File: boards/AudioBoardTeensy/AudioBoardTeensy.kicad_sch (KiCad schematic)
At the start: 7 parts, among them J1 AudioJack2_Ground, U1 Teensy4.0

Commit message: Schematic draft
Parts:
- added H1, H2, H3, H4: MountingHole_Pad, symbol Mechanical:MountingHole_Pad
- added J2, J3, J4: Conn_01x20_Pin, Connector_PinHeader_2.54mm:PinHeader_1x20_P2.54mm_Vertical, symbol Connector:Conn_01x20_Pin
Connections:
- net +3V3: now also J2.2 (Pin_2), J3.1 (Pin_1), J3.10 (Pin_10), J3.11 (Pin_11), J3.12 (Pin_12), J3.13 (Pin_13), J3.14 (Pin_14), J3.15 (Pin_15), J3.16 (Pin_16), J3.17 (Pin_17), J3.18 (Pin_18), J3.19 (Pin_19), J3.2 (Pin_2), J3.20 (Pin_20), J3.3 (Pin_3), J3.4 (Pin_4), J3.5 (Pin_5), J3.6 (Pin_6), J3.7 (Pin_7), J3.8 (Pin_8), J3.9 (Pin_9)
- net GND: now also J2.1 (Pin_1), J2.20 (Pin_20)
- net MOSI: now reaches U1.13 (11_MOSI_CTX1)
- net MOSI: now also J2.8 (Pin_8)
- net MISO: now reaches U1.14 (12_MISO_MQSL)
- net MISO: now also J2.4 (Pin_4)
- net CS: now reaches U1.2 (0_RX1_CRX2_CS1)
- net CS: now also J2.15 (Pin_15)
- net SCK: now reaches U1.20 (13_SCK_CRX1_LED)
- net SCK: now also J2.7 (Pin_7)
- net RST: now reaches U1.3 (1_TX1_CTX2_MISO1)
- net RST: now also J2.16 (Pin_16)
- new net LED1: J4.1 (Pin_1)
- new net LED10: J4.10 (Pin_10)
- new net LED11: J4.11 (Pin_11)
- new net LED12: J4.12 (Pin_12)
- new net LED13: J4.13 (Pin_13)
- new net LED14: J4.14 (Pin_14)
- new net LED15: J4.15 (Pin_15)
- new net LED16: J4.16 (Pin_16)
- new net LED17: J4.17 (Pin_17)
- new net LED18: J4.18 (Pin_18)
- new net LED19: J4.19 (Pin_19)
- new net LED2: J4.2 (Pin_2)
- new net LED20: J4.20 (Pin_20)
- new net LED3: J4.3 (Pin_3)
- new net LED4: J4.4 (Pin_4)
- new net LED5: J4.5 (Pin_5)
- new net LED6: J4.6 (Pin_6)
- new net LED7: J4.7 (Pin_7)
- new net LED8: J4.8 (Pin_8)
- new net LED9: J4.9 (Pin_9)
- no-connect marks 1 -> 17
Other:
- note added: "LEFT"
- note added: "MOUNT HOLES"
- note added: "RIGHT"
- moved on the sheet: U1

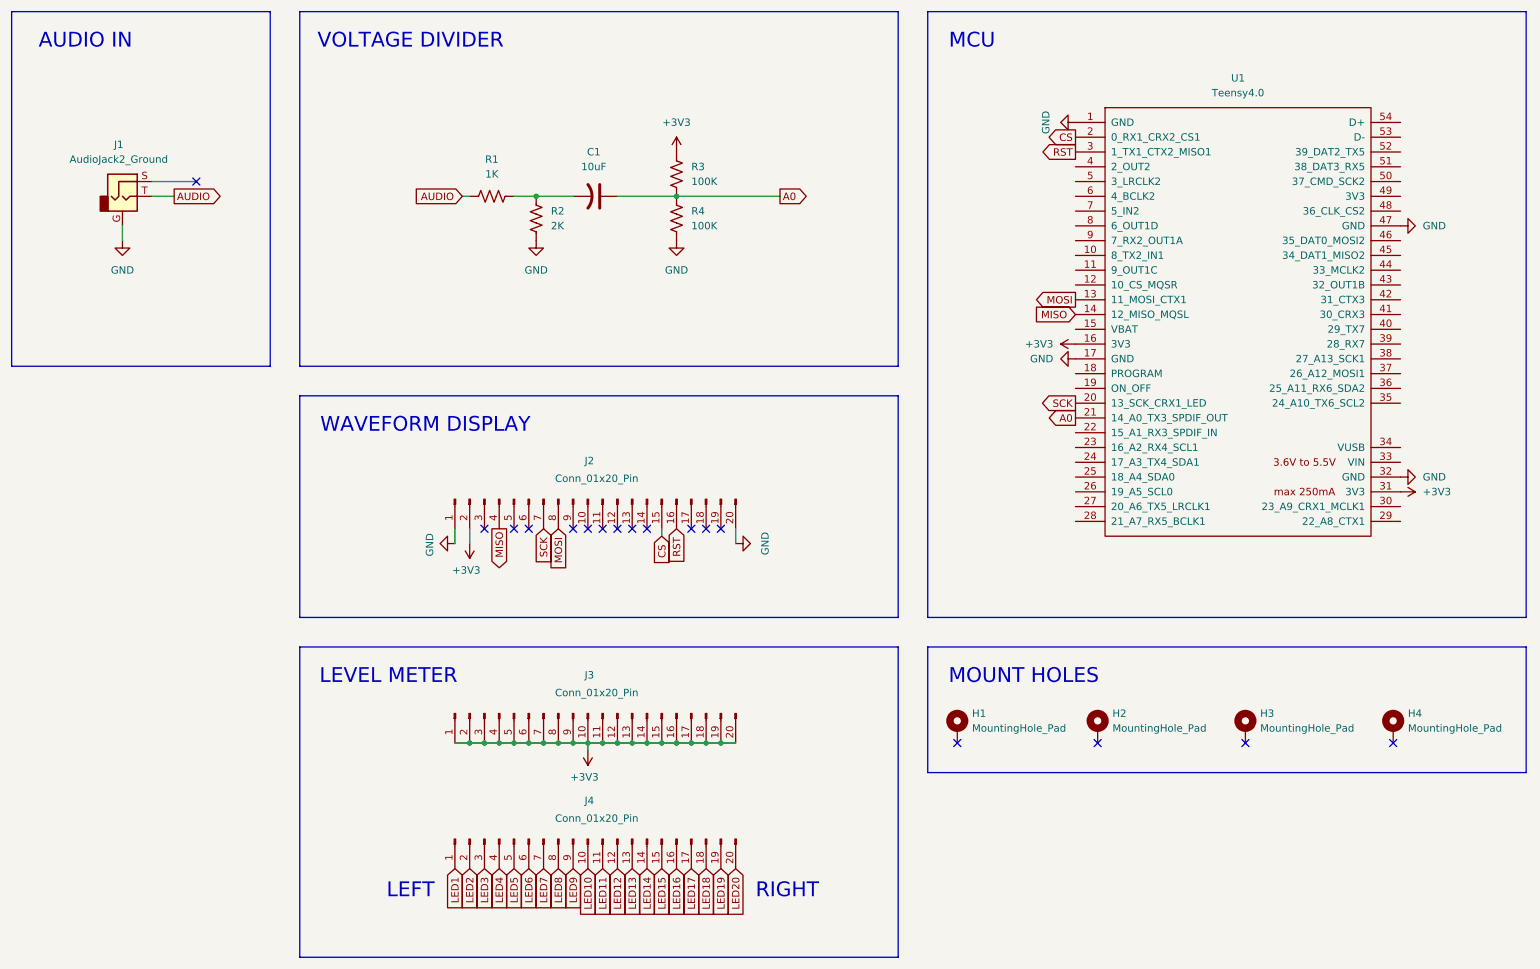
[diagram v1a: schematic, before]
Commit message: Develop audio board readme
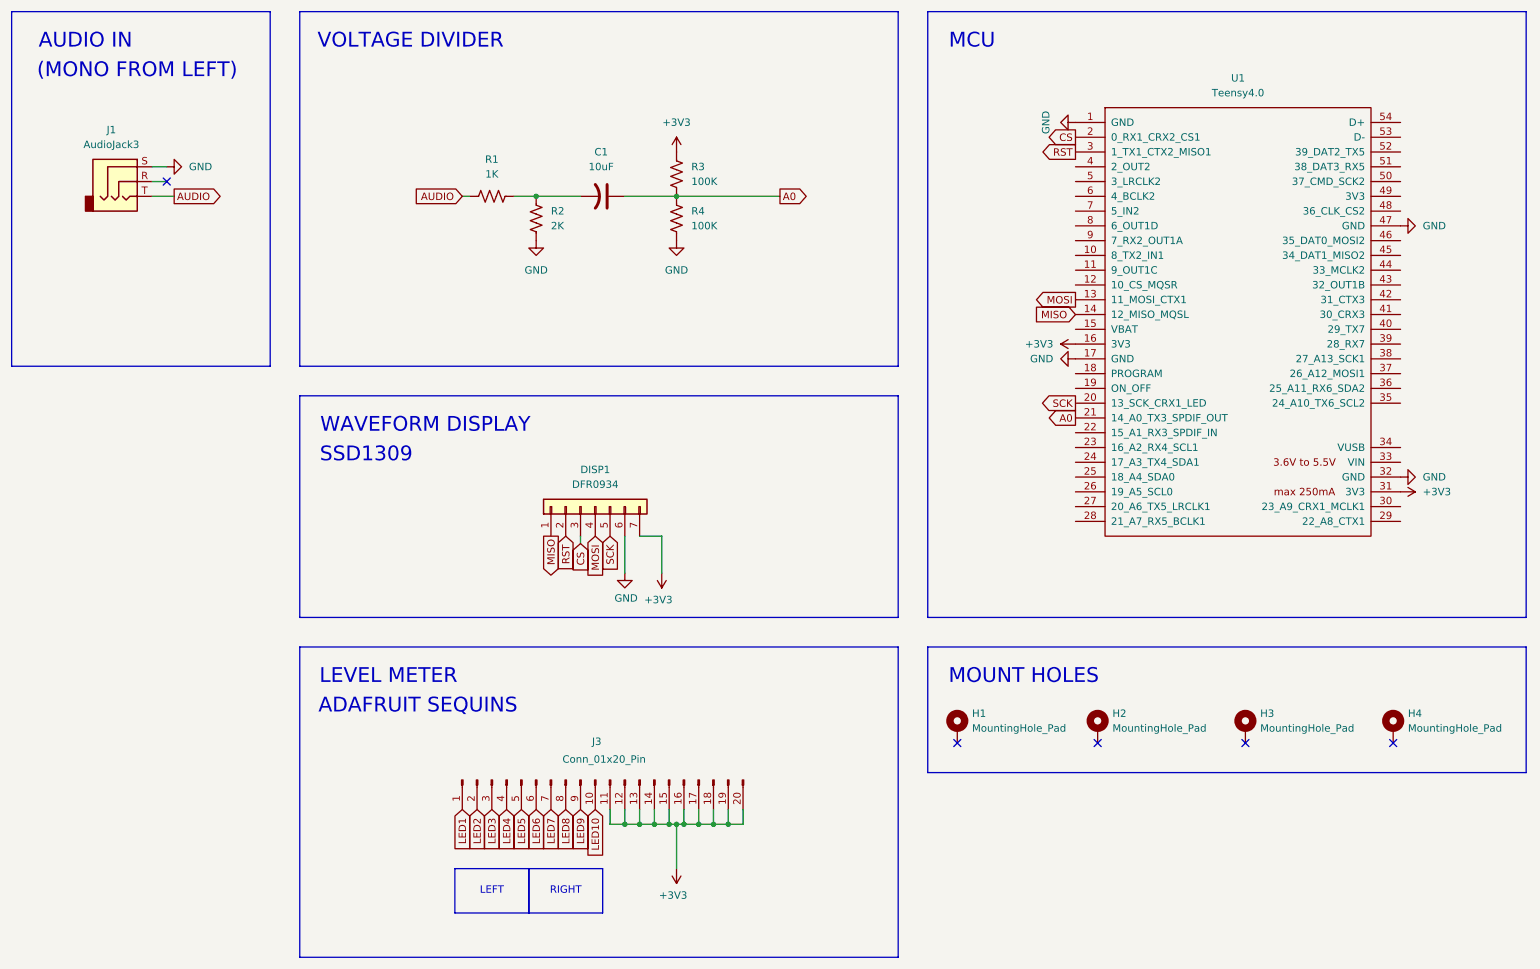
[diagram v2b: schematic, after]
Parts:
- removed J1: AudioJack2_Ground, symbol Connector_Audio:AudioJack2_Ground
- removed J2, J3: Conn_01x20_Pin, Connector_PinHeader_2.54mm:PinHeader_1x20_P2.54mm_Vertical, symbol Connector:Conn_01x20_Pin
- added DISP1: DFR0934, Connector_PinHeader_2.54mm:PinHeader_1x07_P2.54mm_Vertical, symbol Connector_Generic:Conn_01x07
- added J1: AudioJack3, symbol Connector_Audio:AudioJack3
- renumbered J4 to J3
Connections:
- net LED11 is gone; now on net +3V3: J3.11 (Pin_11)
- net LED12 is gone; now on net +3V3: J3.12 (Pin_12)
- net LED13 is gone; now on net +3V3: J3.13 (Pin_13)
- net LED14 is gone; now on net +3V3: J3.14 (Pin_14)
- net LED15 is gone; now on net +3V3: J3.15 (Pin_15)
- net LED16 is gone; now on net +3V3: J3.16 (Pin_16)
- net LED17 is gone; now on net +3V3: J3.17 (Pin_17)
- net LED18 is gone; now on net +3V3: J3.18 (Pin_18)
- net LED19 is gone; now on net +3V3: J3.19 (Pin_19)
- net LED20 is gone; now on net +3V3: J3.20 (Pin_20)
- net +3V3: now also DISP1.7 (Pin_7)
- net AUDIO: now also J1.T
- net CS: now also DISP1.3 (Pin_3)
- net GND: now also DISP1.6 (Pin_6), J1.S
- net MISO: now also DISP1.1 (Pin_1)
- net MOSI: now also DISP1.4 (Pin_4)
- net RST: now also DISP1.2 (Pin_2)
- net SCK: now also DISP1.5 (Pin_5)
- no-connect marks 17 -> 5
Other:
- note added: "(MONO FROM LEFT)"
- note added: "ADAFRUIT SEQUINS"
- note added: "SSD1309"
- moved on the sheet: C1, J3
